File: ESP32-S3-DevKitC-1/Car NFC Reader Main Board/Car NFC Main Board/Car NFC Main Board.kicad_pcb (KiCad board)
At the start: 2 copper layers, 133.1 x 119.9 mm, 13 parts

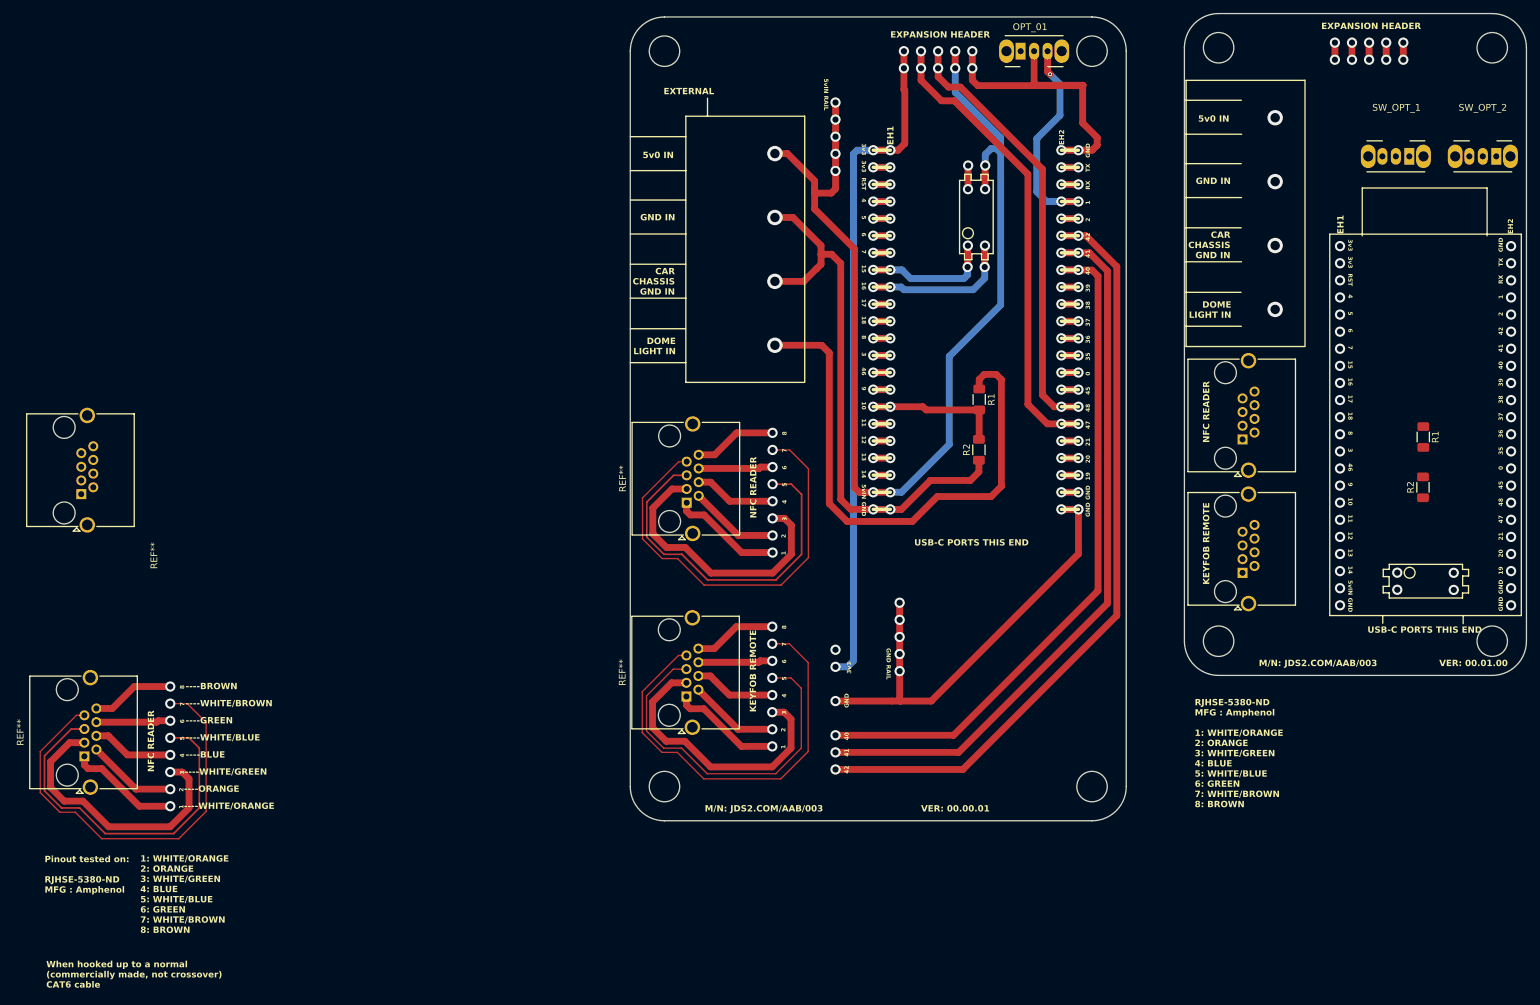
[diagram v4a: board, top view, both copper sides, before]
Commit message: NFC reader board version submitted to JLCPCB
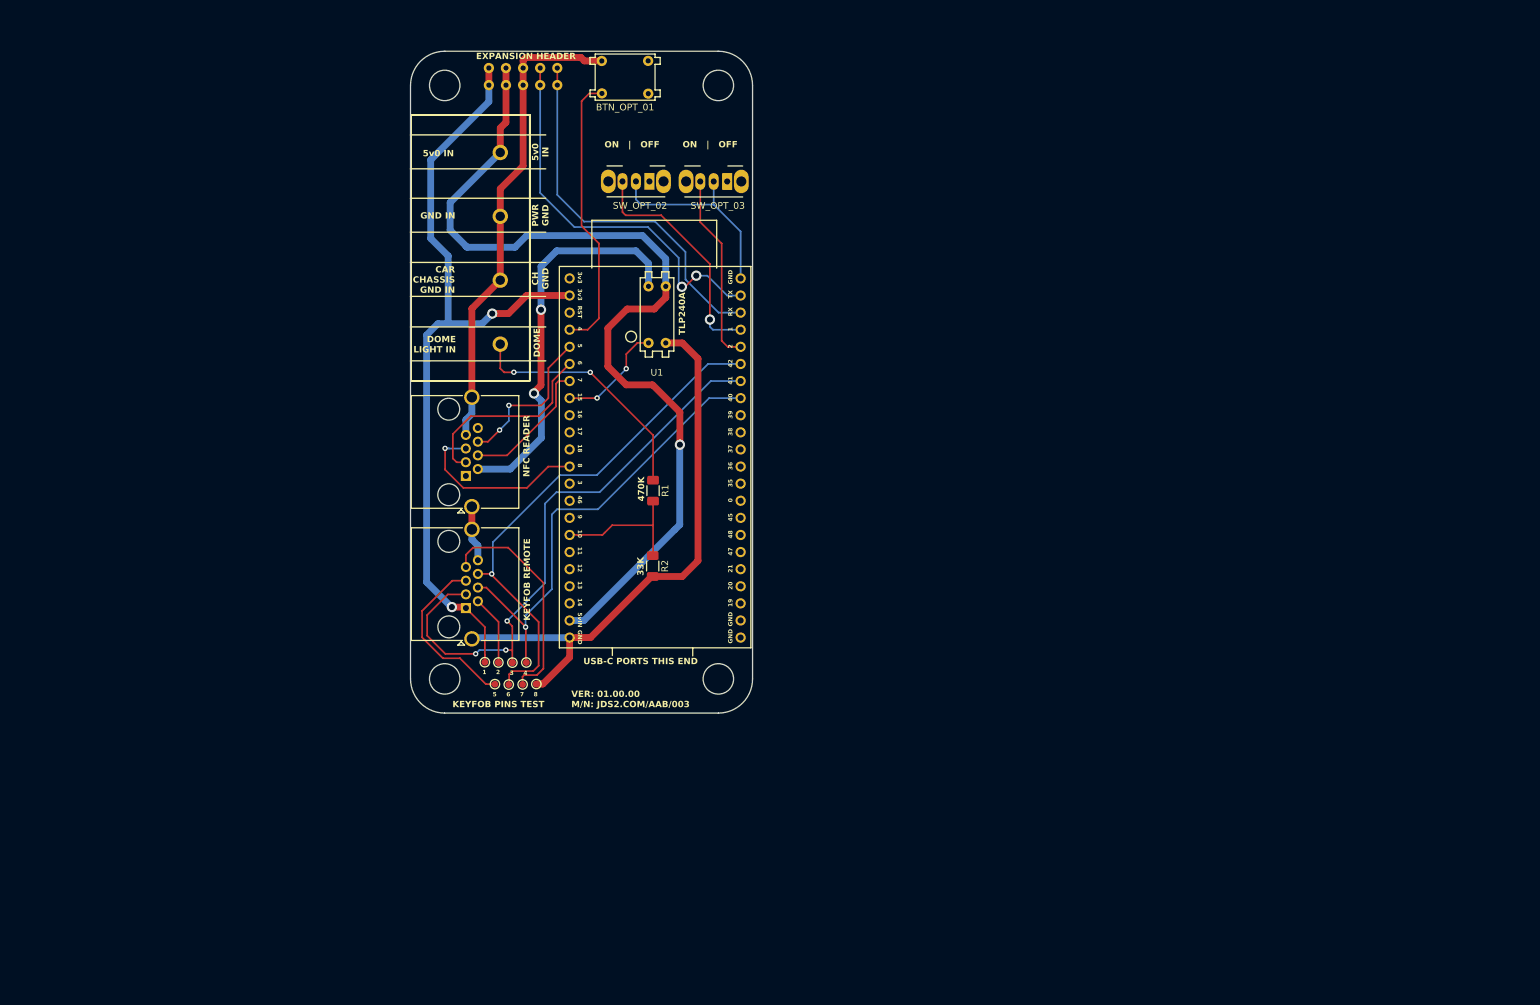
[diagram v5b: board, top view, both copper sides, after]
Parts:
- removed OPT_01: SW_Slide_SPDT_Angled_CK_OS102011MA1Q, Button_Switch_THT:SW_Slide_SPDT_Angled_CK_OS102011MA1Q
- removed the R1 at (171.2, 97.5)
- removed the R1 at (237.1, 103.0)
- removed the R2 at (237.1, 110.5)
- removed the R2 at (171.2, 104.9)
- removed the REF** at (127.8, 112.8)
- removed the REF** at (38.3, 150.5)
- removed the REF** at (37.8, 111.5)
- removed the REF** at (210.3, 103.4)
- removed the REF** at (127.7, 141.6)
- removed the REF** at (210.3, 123.2)
- removed SW_OPT_1, SW_OPT_2: SW_SPDT, Button_Switch_THT:SW_CuK_OS102011MA1QN1_SPDT_Angled
- added BTN_OPT_01: SW_Push_Momentary, Footprint_Library:MOMENTARY_BUTTON, F.Cu at (118.6, 54.5)
- added J1: ~, Footprint_Library:YK441 Screw Terminal Block_CAR_NFC, F.Cu at (95.9, 75.5)
- added J2: AMPHENOL_RJHSE-5380-ND, Connector_RJ:RJ45_Amphenol_RJHSE5380, F.Cu at (95.0, 128.4)
- added J3: AMPHENOL_RJHSE-5380-ND, Connector_RJ:RJ45_Amphenol_RJHSE5380, F.Cu at (95.0, 108.8)
- added J4: 10_PIN_HEADER, Footprint_Library:8_PIN_HEADER, F.Cu at (103.5, 53.3)
- added R1: R, Resistor_SMD:R_1206_3216Metric_Pad1.30x1.75mm_HandSolder, F.Cu at (122.8, 111.0)
- added R2: R, Resistor_SMD:R_1206_3216Metric_Pad1.30x1.75mm_HandSolder, F.Cu at (122.7, 122.2)
- added REF**: TestPoint_Pad_D1.0mm, TestPoint:TestPoint_Pad_D1.0mm, F.Cu at (101.3, 139.8)
- added REF**: TestPoint_Pad_D1.0mm, TestPoint:TestPoint_Pad_D1.0mm, F.Cu at (99.8, 136.5)
- added REF**: TestPoint_Pad_D1.0mm, TestPoint:TestPoint_Pad_D1.0mm, F.Cu at (99.3, 139.7)
- added REF**: TestPoint_Pad_D1.0mm, TestPoint:TestPoint_Pad_D1.0mm, F.Cu at (97.8, 136.5)
- added REF**: TestPoint_Pad_D1.0mm, TestPoint:TestPoint_Pad_D1.0mm, F.Cu at (103.9, 136.5)
- added REF**: TestPoint_Pad_D1.0mm, TestPoint:TestPoint_Pad_D1.0mm, F.Cu at (101.9, 136.5)
- added REF**: TestPoint_Pad_D1.0mm, TestPoint:TestPoint_Pad_D1.0mm, F.Cu at (103.4, 139.8)
- added REF**: TestPoint_Pad_D1.0mm, TestPoint:TestPoint_Pad_D1.0mm, F.Cu at (105.4, 139.7)
- added SW_OPT_02: SW_SPDT, Button_Switch_THT:SW_CuK_OS102011MA1QN1_SPDT_Angled, F.Cu at (122.2, 65.1)
- added SW_OPT_03: SW_SPDT, Button_Switch_THT:SW_CuK_OS102011MA1QN1_SPDT_Angled, F.Cu at (133.8, 65.1)
- added U1: TLP240A, Footprint_Library:TLP240A, F.Cu at (123.3, 84.7)
- added U2: ESP32-S3-DevKitC-1_DAVID, Footprint_Library:ESP32-S3-DEVKITC_DAVID, F.Cu at (123.1, 102.3)
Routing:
- net (no net): track 1351.9 -> 0.00 mm, vias 167 -> 0
- net +5V: track 0.00 -> 137.2 mm, vias 0 -> 1
- net +3.3V: track 0.00 -> 119.9 mm, vias 0 -> 2
- net GND: track 303.5 -> 193.8 mm, vias 27 -> 0
- net TX: track 99.5 -> 0.00 mm, vias 14 -> 0
- net Net-(J2-3/WHT-GREEN): track 0.00 -> 86.9 mm, vias 0 -> 3
- net Net-(J2-6/GREEN): track 0.00 -> 77.2 mm, vias 0 -> 1
- net Net-(J2-4/BLUE): track 0.00 -> 68.3 mm, vias 0 -> 1
- net Net-(J3-2/ORANGE): track 0.00 -> 58.8 mm, vias 0 -> 2
- net Net-(J4-TX0): track 0.00 -> 58.3 mm, vias 0 -> 2
- net Net-(J4-RX0): track 0.00 -> 55.7 mm
- net /DOME: track 81.0 -> 37.1 mm
- net Net-(U2-GPIO4_TOUCH4/ADC1_CH3/RTC): track 0.00 -> 41.9 mm
- net Net-(SW_OPT_02-C): track 0.00 -> 34.8 mm, vias 0 -> 1
- net unconnected-(J2-7/WHT-BROWN-Pad7): track 0.00 -> 33.4 mm
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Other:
- board size 133.1 x 119.9 mm -> 50.8 x 98.3 mm
- board text added: "33K"
- board text added: "470K"
- board text added: "BTN_OPT_01"
- board text added: "KEYFOB PINS TEST"
- board text added: "ON | OFF"
- board text added: "SW_OPT_02"
- board text added: "SW_OPT_03"
- board text added: "TLP240A"
- board text added: "VER: 01.00.00"
- board text removed: "----BLUE"
- board text removed: "----BROWN"
- board text removed: "----GREEN"
- board text removed: "----ORANGE"
- board text removed: "----WHITE/BLUE"
- board text removed: "----WHITE/BROWN"
- board text removed: "----WHITE/GREEN"
- board text removed: "----WHITE/ORANGE"
- board text removed: "1: WHITE/ORANGE 2: ORANGE 3: WHITE/GREEN 4: BLUE 5: WHITE/BLUE 6: GREEN 7: WHITE/BROWN 8: BROWN"
- board text removed: "5v0 IN"
- board text removed: "5vIN RAIL"
- board text removed: "CAR CHASSIS GND IN"
- board text removed: "DOME LIGHT IN"
- board text removed: "EH1"
- board text removed: "EH2"
- board text removed: "EXTERNAL"
- board text removed: "GND IN"
- board text removed: "GND RAIL"
- board text removed: "Pinout tested on: RJHSE-5380-ND MFG : Amphenol"
- board text removed: "RJHSE-5380-ND MFG : Amphenol 1: WHITE/ORANGE 2: ORANGE 3: WHITE/GREEN 4: BLUE 5: WHITE/BLUE 6: GREEN 7: WHITE/BROWN 8: BROWN"
- board text removed: "USB-C PORTS THIS END"
- board text removed: "VER: 00.00.01"
- board text removed: "VER: 00.01.00"
- board text removed: "When hooked up to a normal (commercially made, not crossover) CAT6 cable"

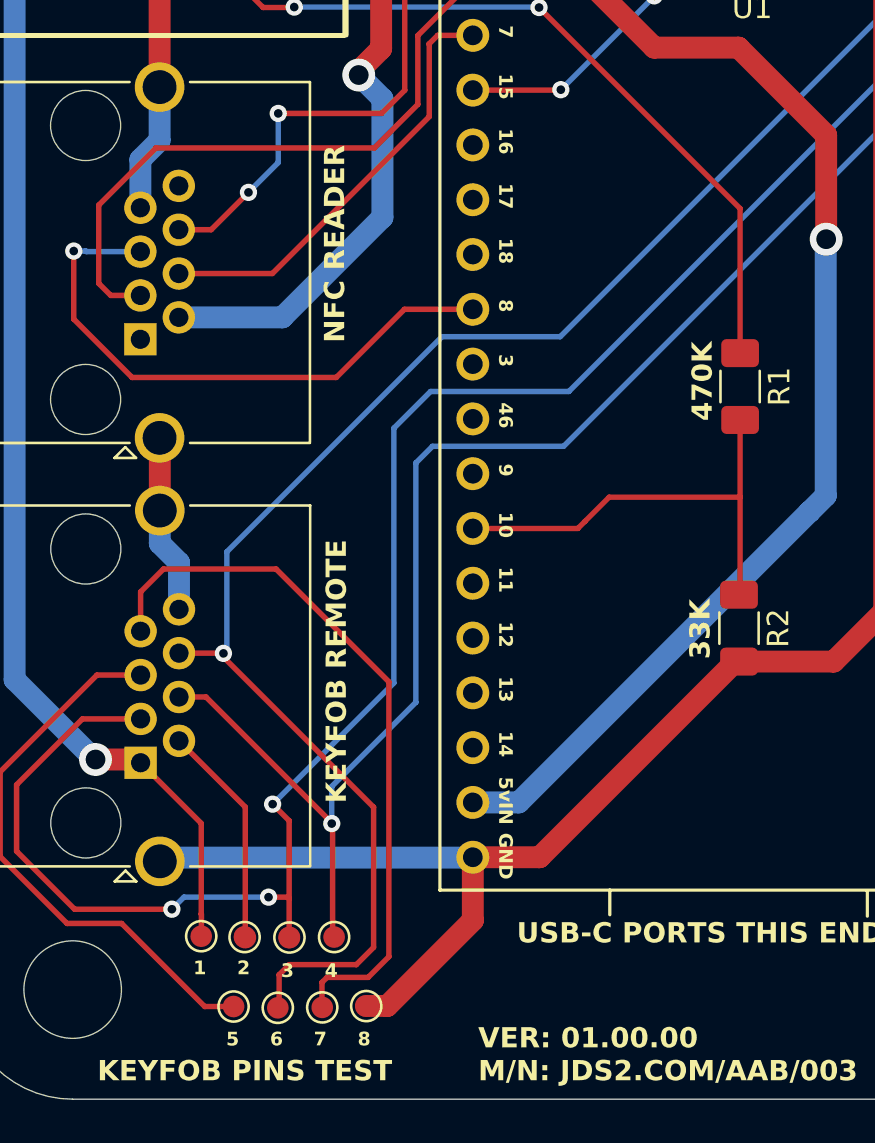
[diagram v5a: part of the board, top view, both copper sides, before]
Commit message: Fixed PCB and schematic where GND pin on NFC reader ethernet port went to pin 7 instead of pin 8 like it should have
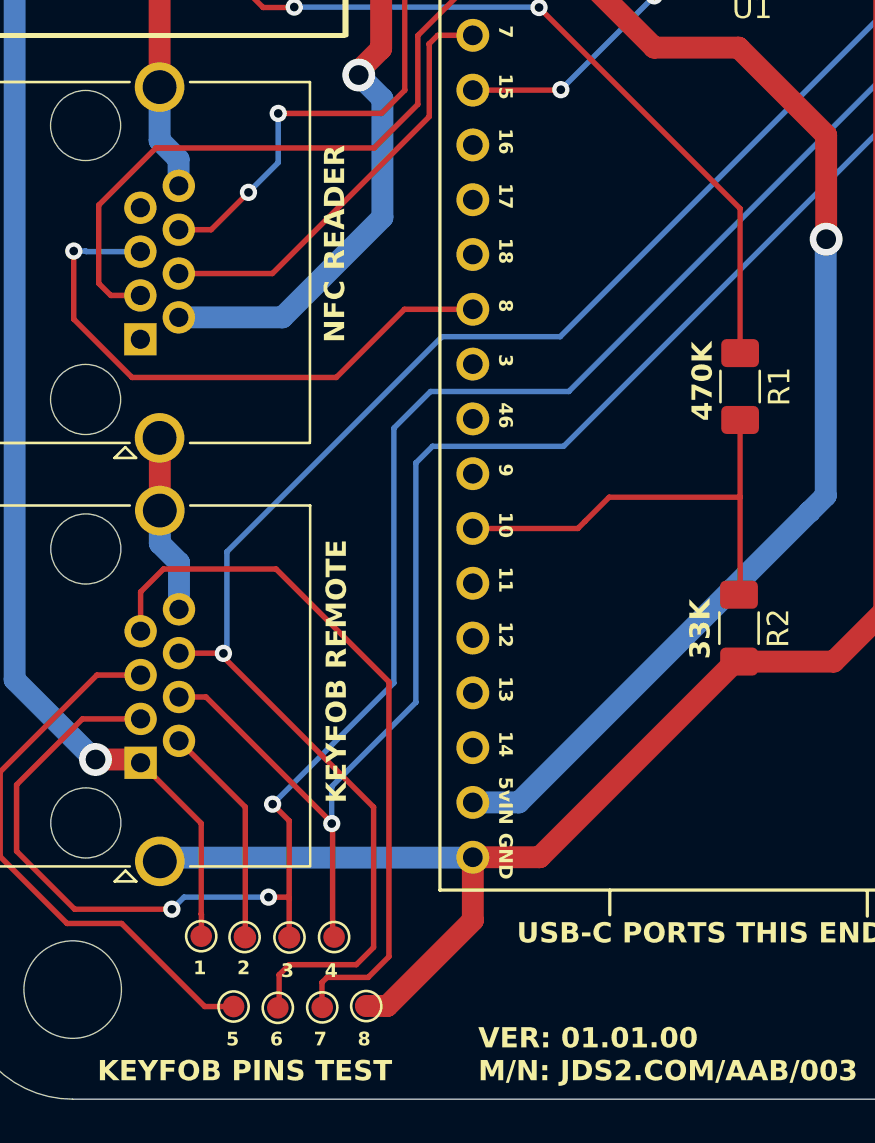
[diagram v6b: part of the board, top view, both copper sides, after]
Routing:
- net GND: track 193.8 -> 192.8 mm
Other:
- board text added: "VER: 01.01.00"
- board text removed: "VER: 01.00.00"
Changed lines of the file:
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@@
 		)
 	)
-	(gr_text "VER: 01.00.00"
+	(gr_text "VER: 01.01.00"
 		(at 110.617 141.739862 0)
 		(layer "F.SilkS")
@@
 	)
 	(segment
-		(start 95.85 99.58)
-		(end 94.96 100.47)
+		(start 96.73 100.46)
+		(end 96.73 101.63)
 		(width 1.016)
 		(layer "B.Cu")
@@
 	)
 	(segment
-		(start 94.96 100.47)
-		(end 94.96 102.704)
-		(width 1.016)
-		(layer "B.Cu")
-		(net 1)
-	)
-	(segment
 		(start 135.77 72.5)
 		(end 135.77 79.47)
@@
 		(width 1.016)
 		(layer "B.Cu")
+		(net 1)
+	)
+	(segment
+		(start 95.85 99.58)
+		(end 96.73 100.46)
+		(width 1.016)
+		(layer "B.Cu")
